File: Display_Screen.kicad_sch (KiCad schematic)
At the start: 0 parts

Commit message: driver controls + lighting architecture
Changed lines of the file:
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@@
 	(generator_version "9.0")
 	(paper "A4")
-	(hierarchical_label "TemperatureTaps"
+	(hierarchical_label "HDMI"
 		(shape input)
-		(at 157.48 92.71 0)
+		(at 158.75 106.68 0)
 		(effects
 			(font

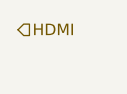
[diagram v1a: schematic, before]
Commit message: add LV pwr dist
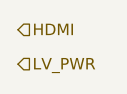
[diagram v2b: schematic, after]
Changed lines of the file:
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@@
 	(generator_version "9.0")
 	(paper "A4")
+	(hierarchical_label "LV_PWR"
+		(shape input)
+		(at 158.75 110.49 0)
+		(effects
+			(font
+				(size 1.27 1.27)
+			)
+			(justify left)
+		)
+	)
 	(hierarchical_label "HDMI"
 		(shape input)

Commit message: wiring stuff
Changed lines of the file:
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@@
 	(generator_version "9.0")
 	(paper "A4")
-	(hierarchical_label "LV_PWR"
+	(hierarchical_label "+12V"
 		(shape input)
 		(at 158.75 110.49 0)
 		(effects
 			(font
+				(size 1.27 1.27)
+			)
+			(justify left)
+		)
+	)
+	(hierarchical_label "GND"
+		(shape input)
+		(at 158.75 114.3 0)
+		(effects
+			(font

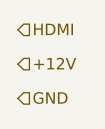
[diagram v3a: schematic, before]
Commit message: Updated Controls + Telemetry
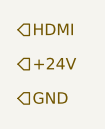
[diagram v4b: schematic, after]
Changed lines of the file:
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@@
 	(generator_version "9.0")
 	(paper "A4")
-	(hierarchical_label "+12V"
+	(hierarchical_label "+24V"
 		(shape input)
 		(at 158.75 110.49 0)
